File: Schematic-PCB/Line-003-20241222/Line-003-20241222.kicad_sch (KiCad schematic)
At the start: 238 parts, among them J2 VIN, J3 Conn_MD, SW1 RESET, U45 ATmega2560-16A, U46 LM393, U47 LM393, U48 LM393, U49 LM393, U50 LM393, U51 LM393, U52 LM393, U53 LM393, U54 LM393, U55 LM393, U56 LM393, U57 LM393, U58 LM393, U59 LM393, U60 LM393, U61 LM393, U62 ATmega2560 Pro Board

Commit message: update: しきい値を2つ使うようにした
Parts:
- removed U45: ATmega2560-16A, Package_QFP:TQFP-100_14x14mm_P0.5mm, symbol MCU_Microchip_ATmega:ATmega2560-16A
- added C26, C6: 0.1uF, symbol Device:C_Small
- added C3: 10uF, Capacitor_SMD:C_0805_2012Metric, symbol Device:C_Small
- added JP4: 160Hz, Jumper:SolderJumper-2_P1.3mm_Open_Pad1.0x1.5mm, symbol Jumper:Jumper_2_Small_Open
- added JP5: 16Hz, Jumper:SolderJumper-2_P1.3mm_Open_Pad1.0x1.5mm, symbol Jumper:Jumper_2_Small_Open
- added JP6: 1.6Hz, Jumper:SolderJumper-2_P1.3mm_Open_Pad1.0x1.5mm, symbol Jumper:Jumper_2_Small_Open
- added R86: 100, Resistor_SMD:R_0603_1608Metric, symbol Device:R_Small
- added R92: 1K, Resistor_SMD:R_0603_1608Metric, symbol Device:R_Small
- added R93: 10K, Resistor_SMD:R_0603_1608Metric, symbol Device:R_Small
- added U63, U64: LM393, symbol Comparator:LM393
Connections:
- net +5V: now also C26.2, C6.2, U63.8 (V+), U64.8 (V+)
- net GND: now also C26.1, C3.2, C6.1, U63.4 (V-), U64.4 (V-)
- net Line-B: now also U64.5 (+)
- net Line-F: now also U63.3 (+)
- net Line-L: now also U63.5 (+)
- net Line-R: now also U64.3 (+)
- new net: JP4.2 (B), R86.1
- new net: JP5.2 (B), R92.1
- new net: JP6.2 (B), R93.1
- new net B: U64.7
- new net F: U63.1
- new net L: U63.7
- new net PWM2: JP4.1 (A), JP5.1 (A), JP6.1 (A)
- new net R: U64.1
- new net Th2: U63.2 (-), U63.6 (-), U64.2 (-), U64.6 (-)
- new net Threshold2: C3.1, R86.2, R92.2, R93.2
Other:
- moved on the sheet: C8, D56, J2, R91

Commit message: update: ラインセンサ基板 ver.003の回路図を更新した
使ってないからbuzzerいらない？
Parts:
- removed C1: 100nF, Capacitor_SMD:C_0603_1608Metric, symbol Device:C_Small
- R82, R87: value 10K -> 1K
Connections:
- net 01: now also U62.D2
- net 02: now also U62.D3
- net 03: now also U62.D4
- net 04: now also U62.D5
- net 05: now also U62.D6
- net 06: now also U62.D7
- net 07: now also U62.D8
- net 08: now also U62.D9
- net 09: now also U62.D10
- net 10: now also U62.D11
- net 11: now also U62.D12
- net 13: now also U62.D14
- net 14: now also U62.D15
- net 15: now also U62.D16
- net 16: now also U62.D17
- net 17: now also U62.D22
- net 18: now also U62.D23
- net 19: now also U62.D24
- net 20: now also U62.D25
- net 21: now also U62.D26
- net 22: now also U62.D27
- net 23: now also U62.D28
- net 24: now also U62.D29
- net B: now also U62.D32
- net F: now also U62.D30
- net L: now also U62.D31
- net LED01: now also U62.D34
- net LED02: now also U62.D35
- net LED03: now also U62.D36
- net MISO: now also U62.MISO
- net MOSI: now also U62.MOSI
- net PWM: now also U62.A0
- net PWM2: now also U62.A1
- net R: now also U62.D33
- net RESET: now also U62.RST
- net RX: now also U62.D19
- net SCK: now also U62.SCK
- net SCL: now also U62.D21
- net SDA: now also U62.D20
- net TX: now also U62.D18
- net 12: now reaches U62.D13
- no-connect marks 22 -> 4
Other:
- moved on the sheet: BZ1, C2, C3, C4, C5, C7, C8, C9, D53, D54, D55, D56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

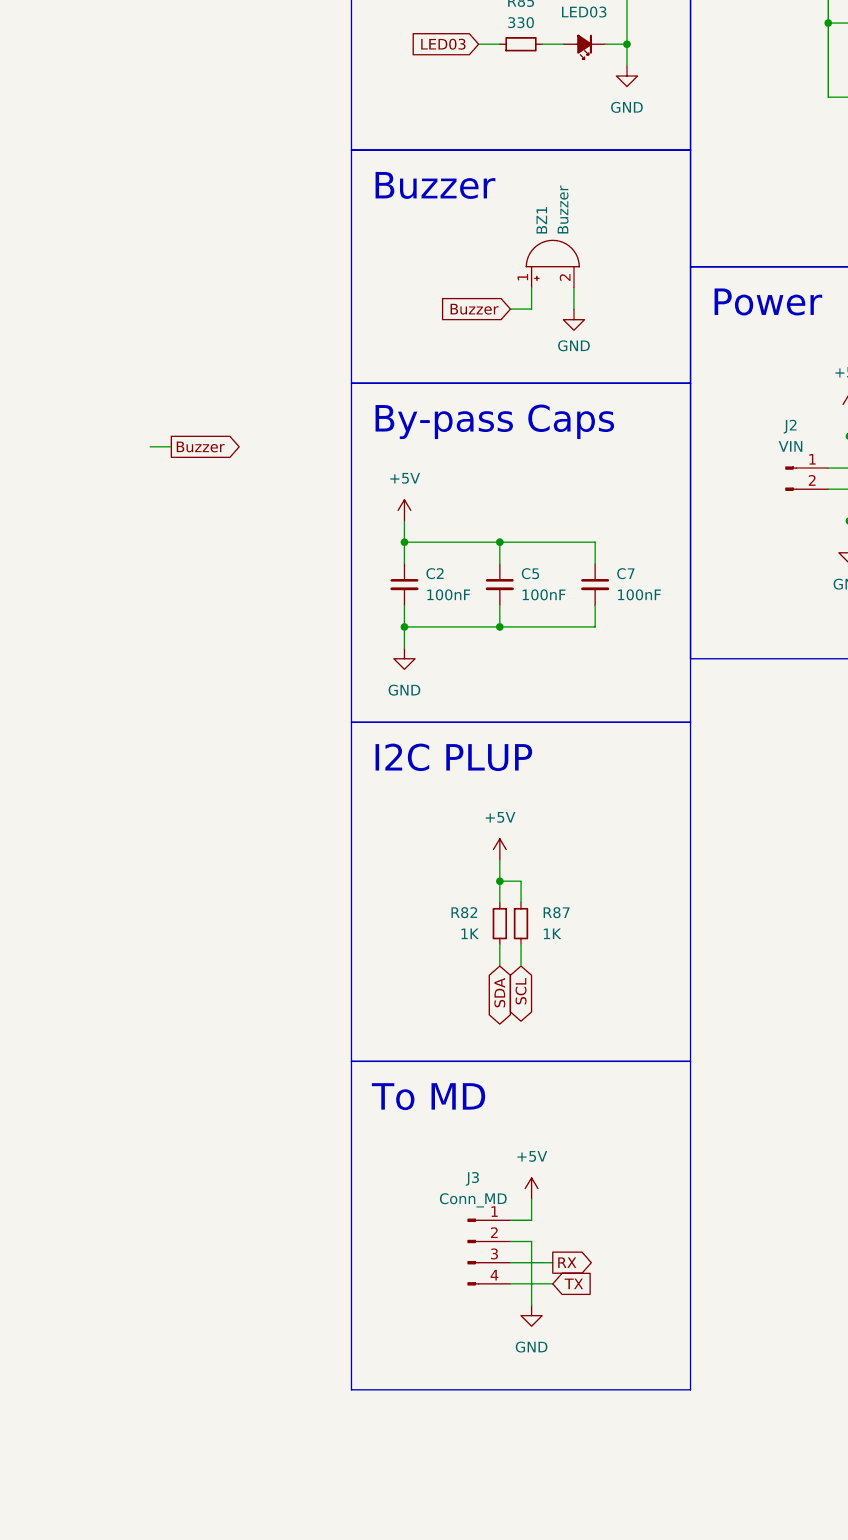
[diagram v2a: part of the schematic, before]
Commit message: update: ブザーをけした
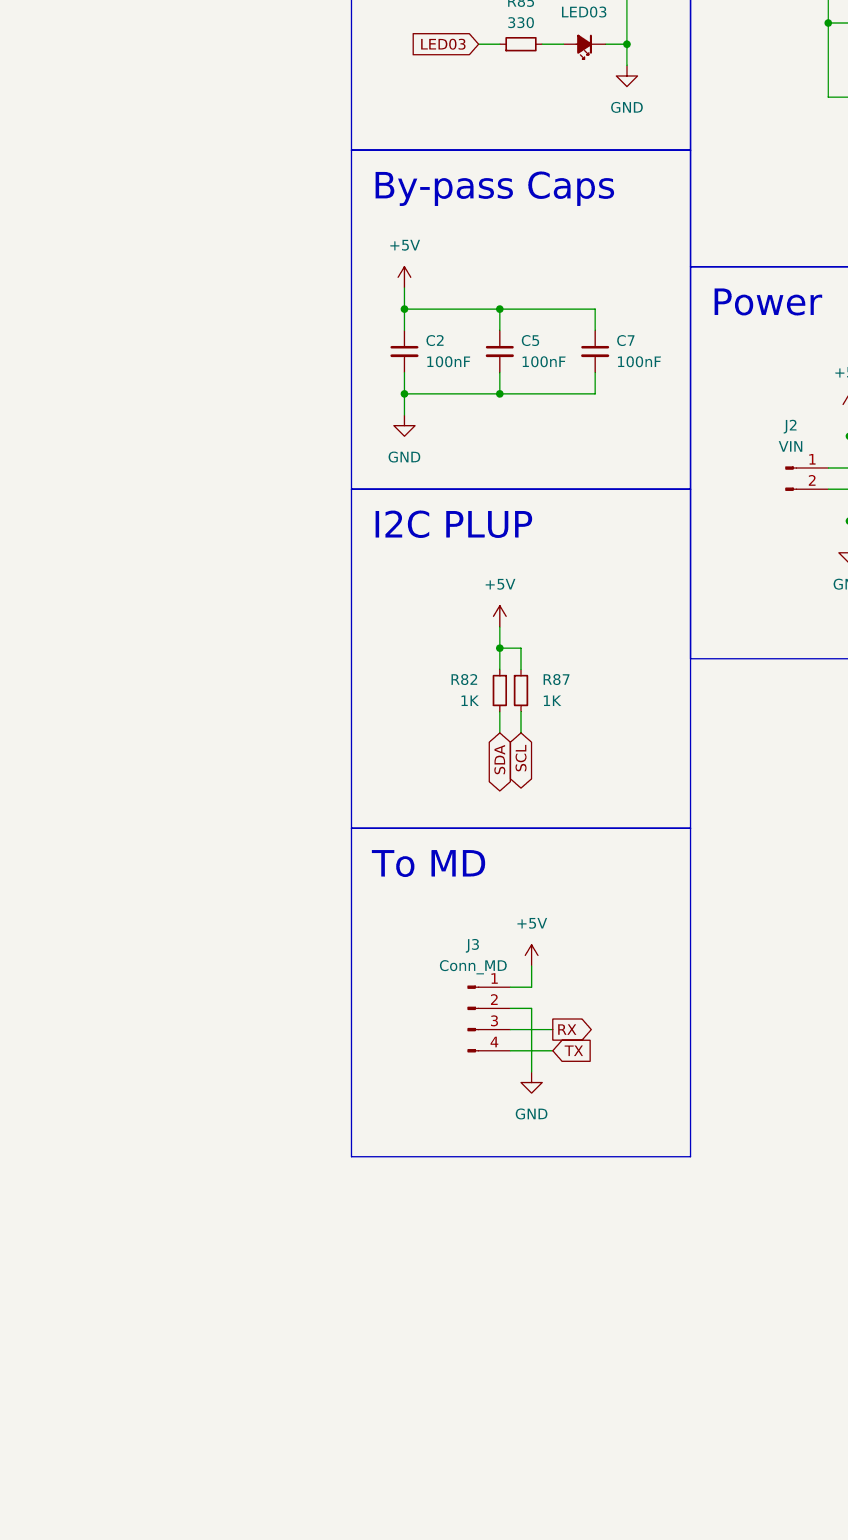
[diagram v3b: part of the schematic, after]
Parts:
- removed BZ1: Buzzer, @2024TOINIOT2-Line:PKM13EPYH4000-A0, symbol Device:Buzzer
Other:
- moved on the sheet: C2, C5, C7, J3, R82, R87

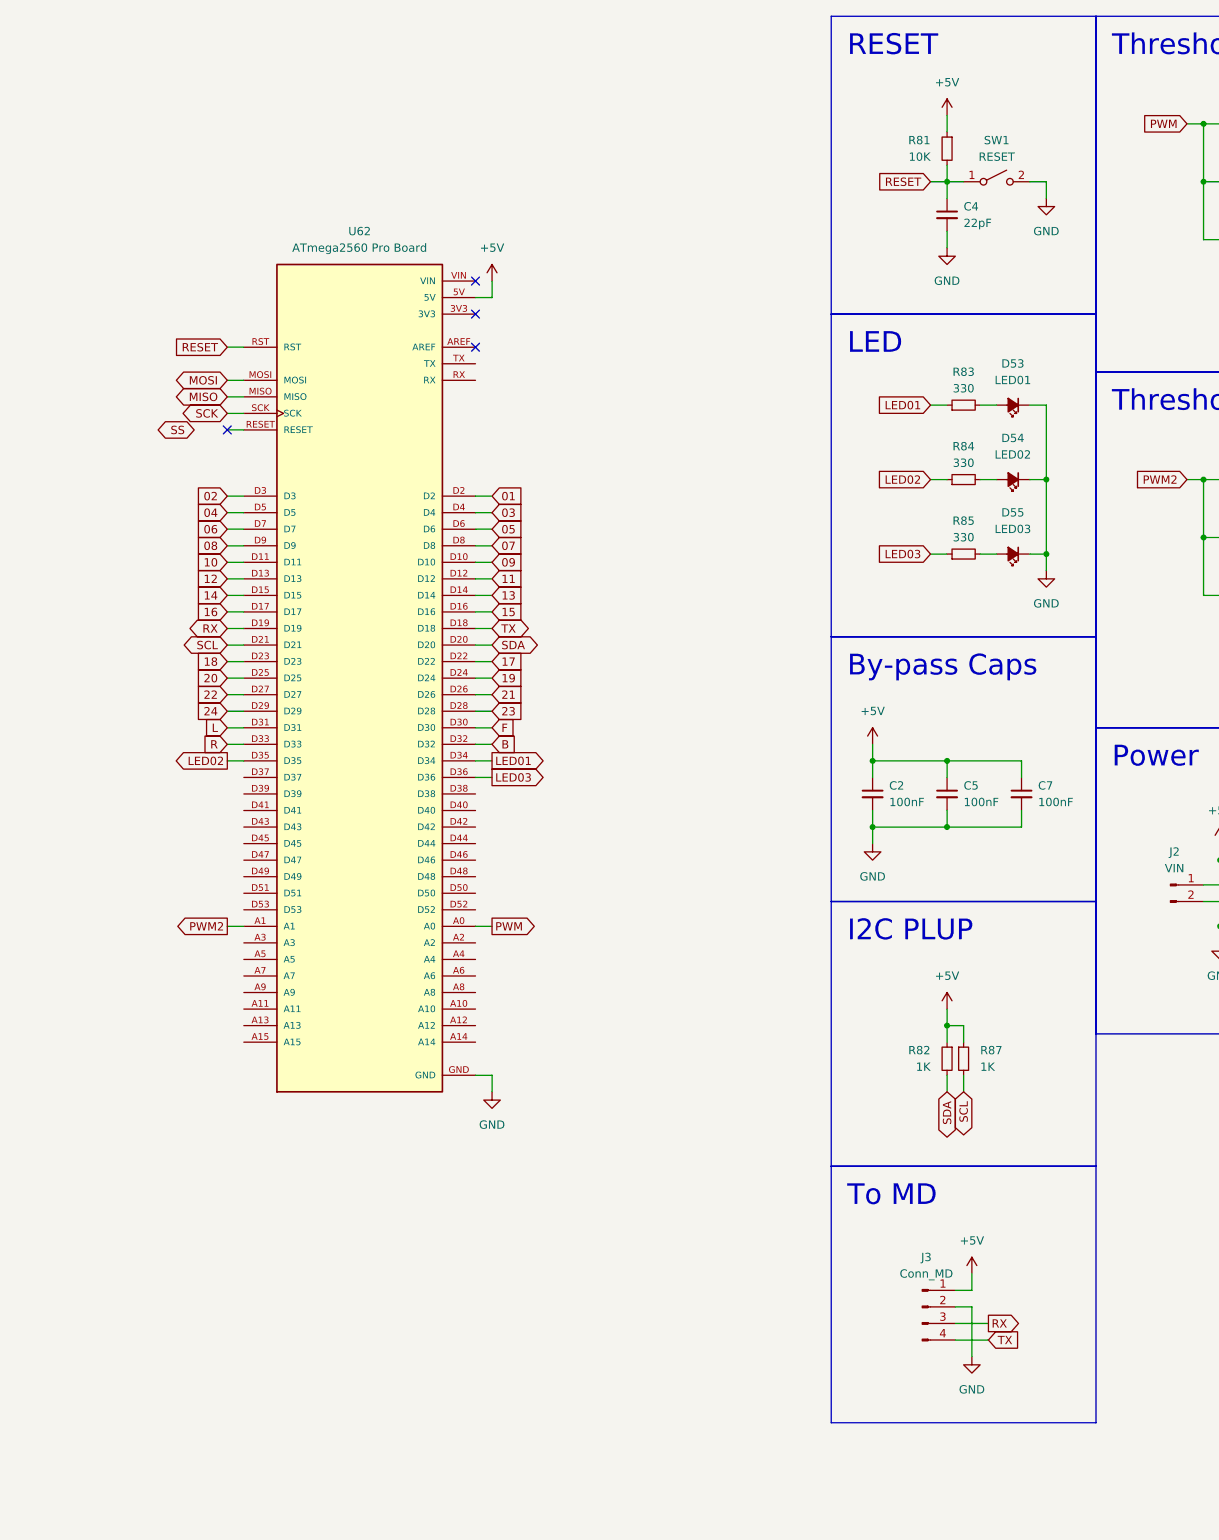
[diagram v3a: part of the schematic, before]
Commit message: update: ラインセンサ基板の回路図を更新した
DRおねがい
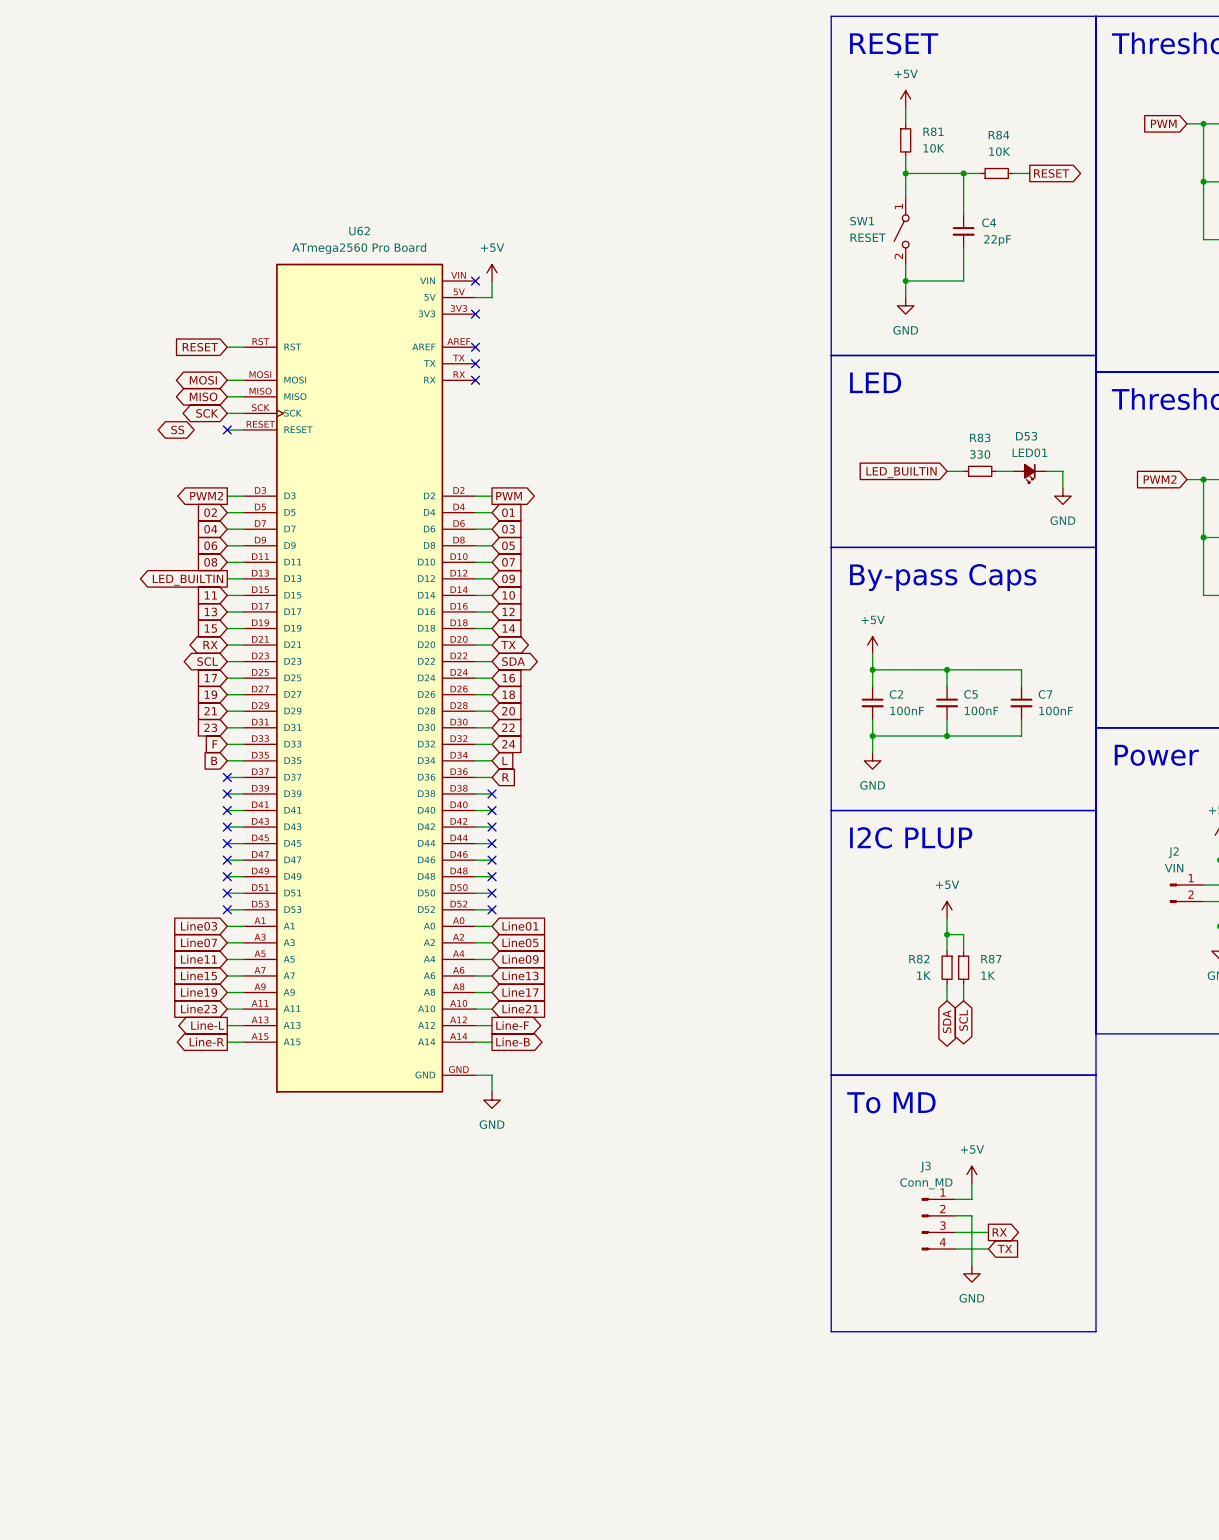
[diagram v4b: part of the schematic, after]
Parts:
- removed D54: LED02, LED_SMD:LED_0603_1608Metric, symbol Device:LED_Small_Filled
- removed D55: LED03, LED_SMD:LED_0603_1608Metric, symbol Device:LED_Small_Filled
- removed R85: 330, Resistor_SMD:R_0603_1608Metric, symbol Device:R_Small
- R84: value 330 -> 10K
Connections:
- net LED03 is gone; now on net R: U62.D36
- net 01: now also U62.D4; no longer U62.D2
- net 02: now also U62.D5; no longer U62.D3
- net 03: now also U62.D6; no longer U62.D4
- net 04: now also U62.D7; no longer U62.D5
- net 05: now also U62.D8; no longer U62.D6
- net 06: now also U62.D9; no longer U62.D7
- net 07: now also U62.D10; no longer U62.D8
- net 08: now also U62.D11; no longer U62.D9
- net 09: now also U62.D12; no longer U62.D10
- net 10: now also U62.D14; no longer U62.D11
- net 11: now also U62.D15; no longer U62.D12
- net 12: now also U62.D16; no longer U62.D13
- net 13: now also U62.D17; no longer U62.D14
- net 14: now also U62.D18; no longer U62.D15
- net 15: now also U62.D19; no longer U62.D16
- net 16: now also U62.D24; no longer U62.D17
- net 17: now also U62.D25; no longer U62.D22
- net 18: now also U62.D26; no longer U62.D23
- net 19: now also U62.D27; no longer U62.D24
- net 20: now also U62.D28; no longer U62.D25
- net 21: now also U62.D29; no longer U62.D26
- net 22: now also U62.D30; no longer U62.D27
- net 23: now also U62.D31; no longer U62.D28
- net 24: now also U62.D32; no longer U62.D29
- net B: now also U62.D35; no longer U62.D32
- net F: now also U62.D33; no longer U62.D30
- net L: now also U62.D34; no longer U62.D31
- net Line-B: now also U62.A14
- net Line-F: now also U62.A12
- net Line-L: now also U62.A13
- net Line-R: now also U62.A15
- net Line01: now also U62.A0
- net Line03: now also U62.A1
- net Line05: now also U62.A2
- net Line07: now also U62.A3
- net Line09: now also U62.A4
- net Line11: now also U62.A5
- net Line13: now also U62.A6
- net Line15: now also U62.A7
- net Line17: now also U62.A8
- net Line19: now also U62.A9
- net Line21: now also U62.A10
- net Line23: now also U62.A11
- net PWM: now also U62.D2; no longer U62.A0
- net PWM2: now also U62.D3; no longer U62.A1
- net R: no longer U62.D33
- net RESET: now also R84.2; no longer C4.1, R81.2, SW1.1 (A)
- net RX: now also U62.D21; no longer U62.D19
- net SCL: now also U62.D23; no longer U62.D21
- net SDA: now also U62.D22; no longer U62.D20
- net TX: now also U62.D20; no longer U62.D18
- net LED01 renamed LED_BUILTIN
- net LED_BUILTIN: now also U62.D13; no longer U62.D34
- net LED02: no longer names the net of R84.1
- net LED02: now also C4.1, R81.2, SW1.1 (A); no longer U62.D35
- no-connect marks 4 -> 23
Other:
- moved on the sheet: C2, C4, C5, C7, D53, J3, R81, R82, R83, R87, SW1

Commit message: update: ラインセンサ基板 ver.003 の回路図を編集・更新した
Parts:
- removed C4: 22pF, Capacitor_SMD:C_0603_1608Metric, symbol Device:C_Small
- removed D45, D46, D47, D48, D49, D50, D51, D52: Wh/Rd, @2024TOINIOT2-Line:LED-3mm, symbol Device:LED_Small_Filled
- removed R73, R74, R75, R76, R77, R78, R79, R80: 75, Resistor_SMD:R_0603_1608Metric, symbol Device:R_Small
- removed R81, R84: 10K, Resistor_SMD:R_0603_1608Metric, symbol Device:R_Small
- added C20: C_Small, symbol Device:C_Small
- added D25, D26: Wh/Rd, @2024TOINIOT2-Line:LED-3mm, symbol Device:LED_Small_Filled
- added R25, R26: Line-PDWN, Resistor_SMD:R_0603_1608Metric, symbol Device:R_Small
- added R55, R56: 75, Resistor_SMD:R_0603_1608Metric, symbol Device:R_Small
- added U25, U26: ~, @2024TOINIOT2-Line:NJL7502L, symbol @2024-Line:NJL7502L
- renumbered C10 to C1, C19 to C10, C20 to C11, C21 to C12, C22 to C13, C23 to C14, C24 to C15, C25 to C16, C6 to C17, C26 to C18, C2 to C19, C11 to C2, C5 to C21, C7 to C22, C8 to C23, C9 to C24, C3 to C25, C12 to C3, C13 to C4, C14 to C5, C15 to C6, C16 to C7, C17 to C8, C18 to C9, D25 to D27, D26 to D28, D27 to D29, D28 to D30, D29 to D31, D30 to D32, D31 to D33, D32 to D34, D33 to D35, D34 to D36, D35 to D37, D36 to D38, D37 to D39, D38 to D40, D39 to D41, D40 to D42, D41 to D43, D42 to D44, D43 to D45, D44 to D46, D53 to D47, D56 to D48, J3 to J1, R25 to R27, R26 to R28, R27 to R29, R28 to R30, R29 to R31, R30 to R32, R31 to R33, R32 to R34, R33 to R35, R34 to R36, R35 to R37, R36 to R38, R37 to R39, R38 to R40, R39 to R41, R40 to R42, R41 to R43, R42 to R44, R43 to R45, R44 to R46, R45 to R47, R46 to R48, R47 to R49, R48 to R50, R49 to R51, R50 to R52, R51 to R53, R52 to R54, R53 to R57, R54 to R58, R55 to R59, R56 to R60, R57 to R61, R58 to R62, R59 to R63, R60 to R64, R61 to R65, R62 to R66, R63 to R67, R64 to R68, R65 to R69, R66 to R70, R67 to R71, R68 to R72, R69 to R73, R70 to R74, R71 to R75, R72 to R76, R82 to R78, R87 to R79, R83 to R80, R88 to R81, R89 to R82, R90 to R83, R86 to R84, R92 to R85, R93 to R86, R91 to R87, U25 to U27, U26 to U28, U27 to U29, U28 to U30, U29 to U31, U30 to U32, U31 to U33, U32 to U34, U33 to U35, U34 to U36, U35 to U37, U36 to U38, U37 to U39, U38 to U40, U39 to U41, U40 to U42, U41 to U43, U42 to U44, U43 to U45, U44 to U46, U46 to U47, U47 to U48, U48 to U49, U49 to U50, U50 to U51, U51 to U52, U52 to U53, U53 to U54, U54 to U55, U55 to U56, U56 to U57, U57 to U58, U58 to U59, U59 to U60, U60 to U61, U61 to U62, U62 to U65
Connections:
- net +5V: now also R55.1, R56.1, U25.2 (Collector), U26.2 (Collector)
- net B: now also U65.D37; no longer U65.D35
- net F: now also U65.D35; no longer U65.D33
- net GND: now also SW1.1 (A), C20.1, D25.1 (K), D26.1 (K), R25.2, R26.2; no longer SW1.2 (B)
- net L: now also U65.D36; no longer U65.D34
- net R: now also U65.D38; no longer U65.D36
- net RESET: now also SW1.2 (B), C20.2
- new net: D25.2 (A), R55.2
- new net: D26.2 (A), R56.2
- new net 25: U65.D33
- new net 26: U65.D34
- new net Line25: R25.1, U25.1 (Emitter)
- new net Line26: R26.1, U26.1 (Emitter)
- no-connect marks 23 -> 21
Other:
- moved on the sheet: C19, C21, C22, D47, J1, R78, R79, R80
